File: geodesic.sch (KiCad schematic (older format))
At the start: 13 parts, among them J1 Program, J10 Hexagon, J11 Hexagon, J2 Pentagon, J3 Pentagon, J4 Pentagon, J5 Pentagon, J6 Pentagon, J7 Hexagon, J8 Hexagon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

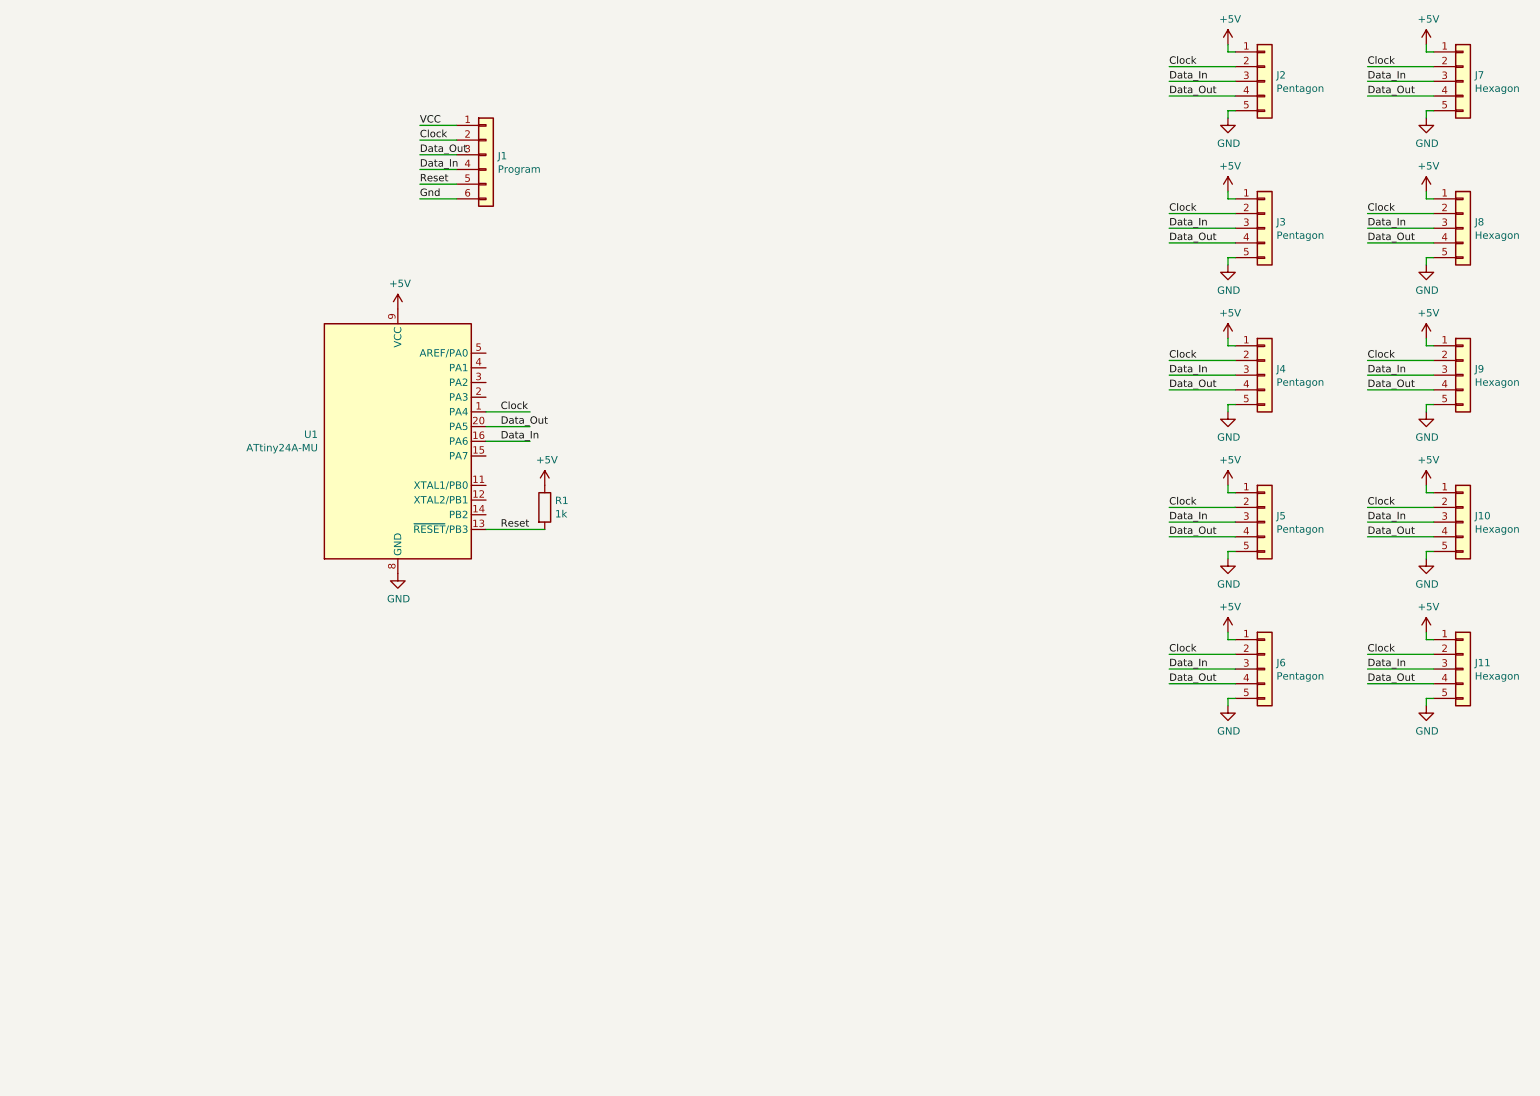
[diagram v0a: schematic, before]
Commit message: Layed out pcb
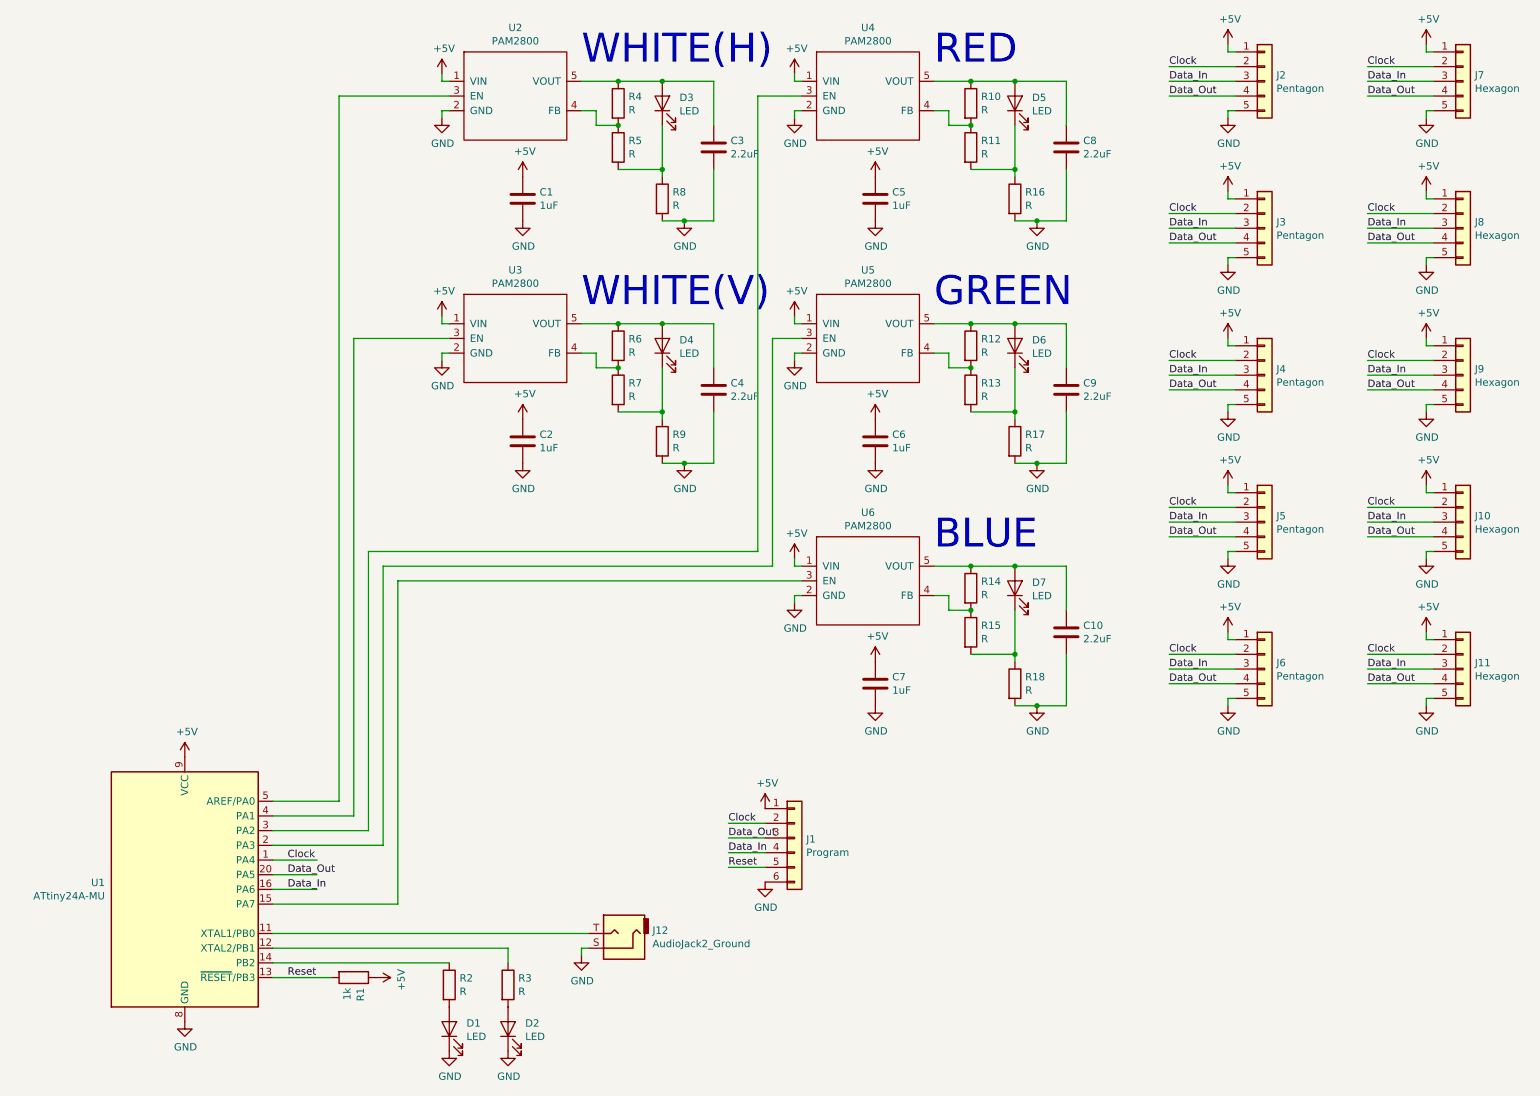
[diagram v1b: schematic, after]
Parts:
- added C1, C2, C5, C6, C7: 1uF, Capacitor_SMD:C_0805_2012Metric_Pad1.15x1.40mm_HandSolder, symbol Device:C
- added C10, C3, C4, C8, C9: 2.2uF, Capacitor_SMD:C_0805_2012Metric_Pad1.15x1.40mm_HandSolder, symbol Device:C
- added D1, D2: LED, LED_SMD:LED_0805_2012Metric_Pad1.15x1.40mm_HandSolder, symbol Device:LED
- added D3, D4: LED, local:XNOVA MP1616, symbol Device:LED
- added D5: LED, LED_SMD:LED_Cree-XQ, symbol Device:LED
- added D6: LED, local:LUXEON_3535L, symbol Device:LED
- added D7: LED, local:Cree_XPE, symbol Device:LED
- added J12: AudioJack2_Ground, Connector_Coaxial:BNC_TEConnectivity_1478204_Vertical, symbol Connector:AudioJack2_Ground
- added R10, R11, R12, R13, R14, R15, R16, R17, R18, R2, R3, R4, R5, R6, R7, R8, R9: R, Resistor_SMD:R_0805_2012Metric_Pad1.15x1.40mm_HandSolder, symbol Device:R
- added U2, U3, U4, U5, U6: PAM2800, Package_TO_SOT_SMD:SOT-23-5_HandSoldering, symbol geodesic:PAM2800
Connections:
- net labels removed: Gnd, VCC
- wire segments 80 -> 188
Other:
- note added: "BLUE"
- note added: "GREEN"
- note added: "RED"
- note added: "WHITE(H)"
- note added: "WHITE(V)"
- moved on the sheet: J1, R1, U1
